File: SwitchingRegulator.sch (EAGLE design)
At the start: 30 parts, among them J1 APP_2POS_CONFIG5V_HORIZ, J2 APP_2POS_CONFIG5V_HORIZ, J4 APP_2POS_CONFIG12V_HORIZ, Q2 Q_CSD18532KCSPCB, Q3 Q_CSD18532KCSPCB, U1 OKI-78SR-5/1.5-W36HC

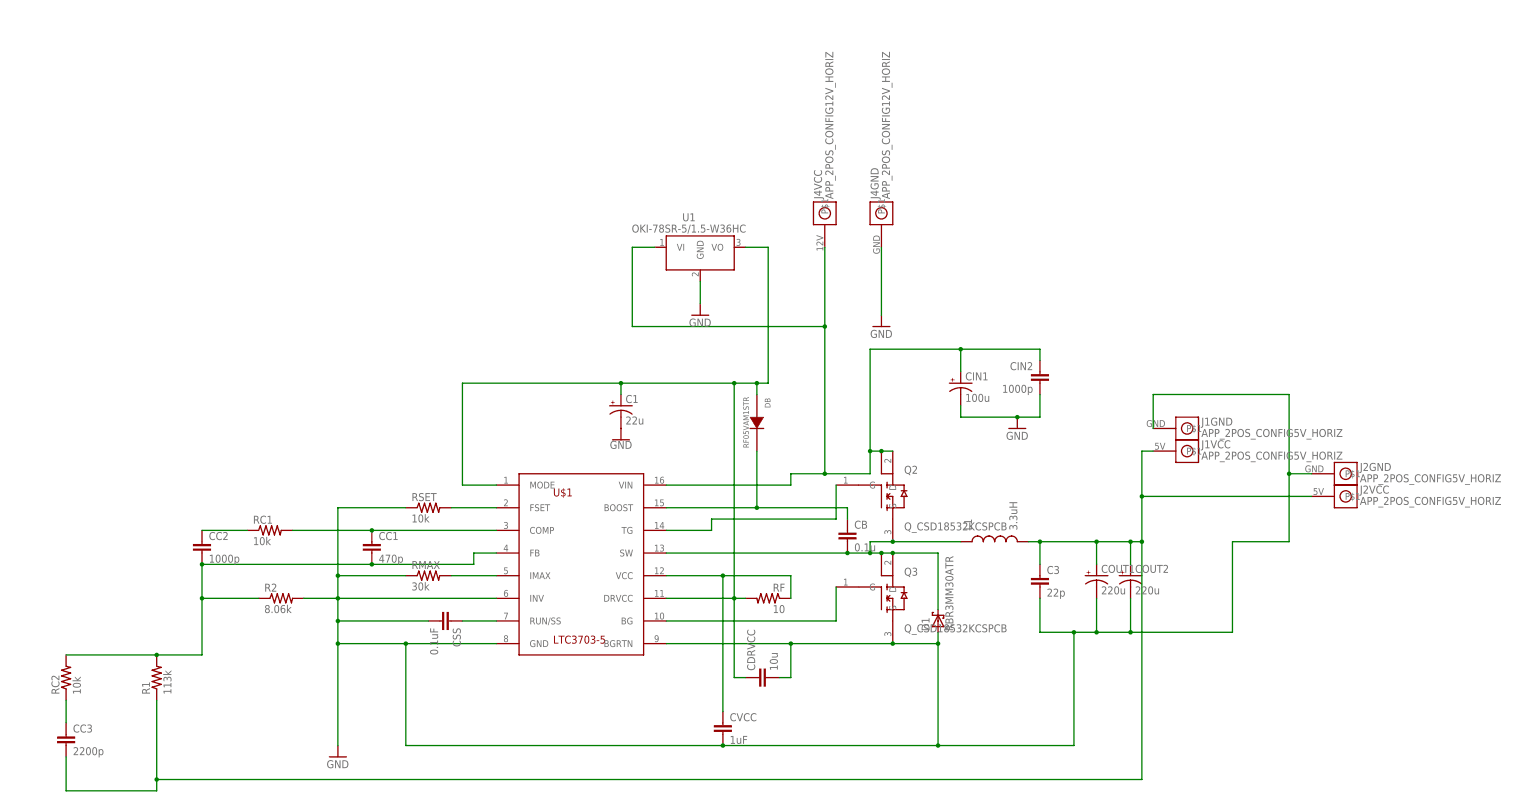
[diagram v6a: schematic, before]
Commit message: Major revision, moved LTC to bottom
Changed signal traces to be much closer to LTC chip.  Modified via stitching to cover whole polygon rather than edges only.  No more vias under IC.  Moved inductor to top side of board to prevent LTC from heating up due to MOSFET heat.  Added silkscreen stuff.  More fine details to come
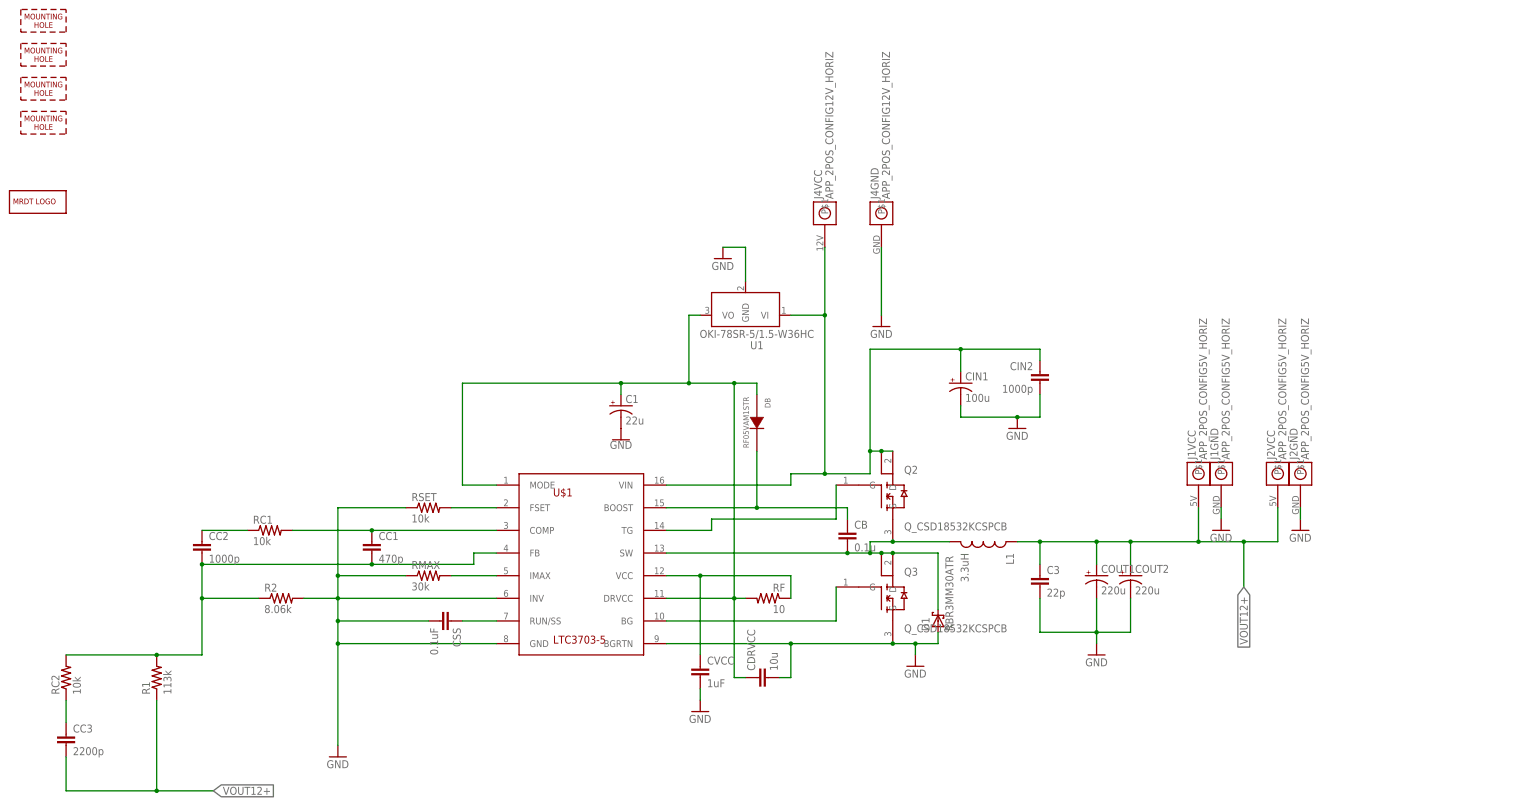
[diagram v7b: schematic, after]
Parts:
- added H1, H2, H3, H4: MOUNTING_HOLE#8, MRDT-Hardware:MOUNTING_HOLE#8
- added LOGO1: MRDT_LOGO, MRDT-Hardware:MRDT_LOGO
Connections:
- net N$15 renamed 5V
- net N$17: now also L1.2; no longer L1.1
- net VOUT12+: now also L1.1; no longer L1.2
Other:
- moved on the sheet: CVCC, J1GND, J1VCC, J2GND, J2VCC, L1, U1

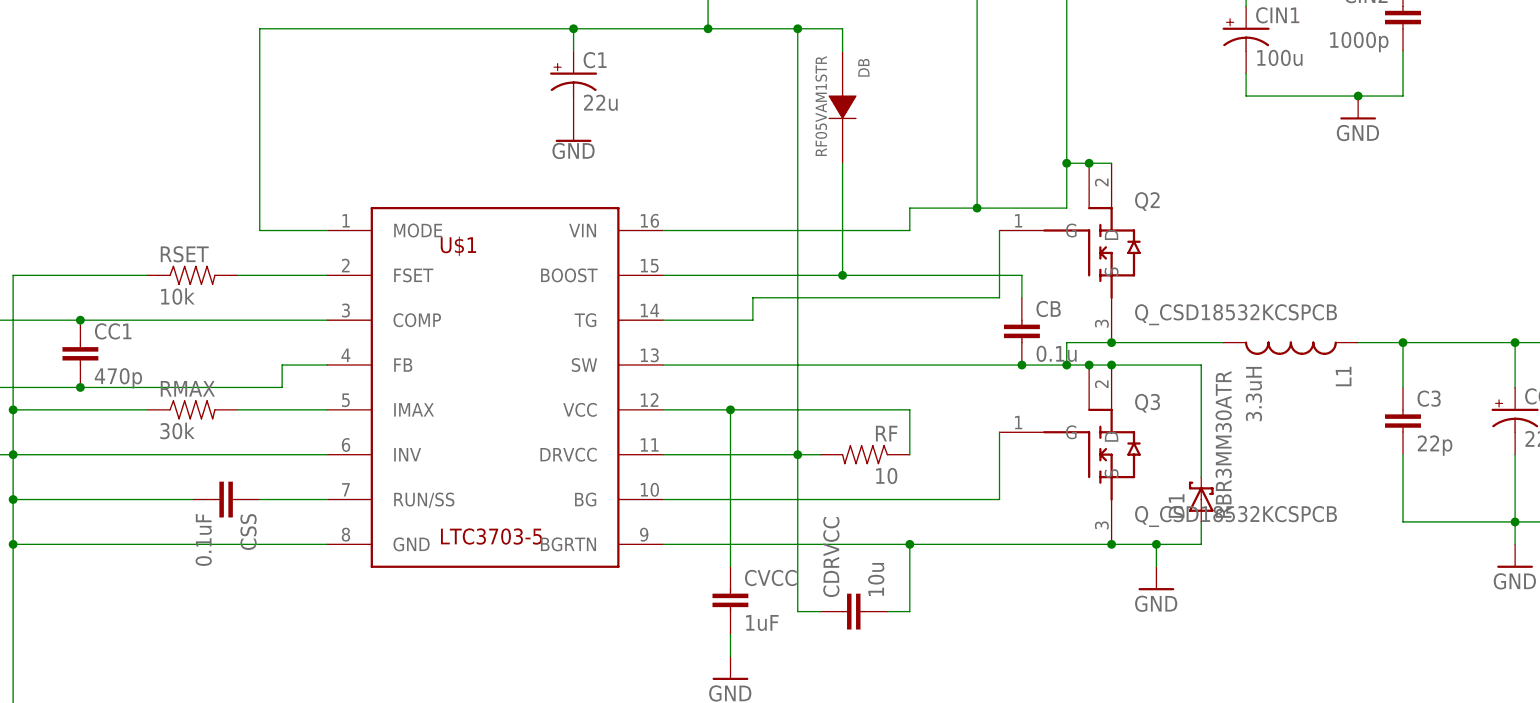
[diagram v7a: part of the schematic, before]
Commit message: Switched to upright mosfets, adjusted board accordingly
Spread out some of the signal components on the bottom side of the board.  Adjusted power planes to compensate for new mosfet orientation.
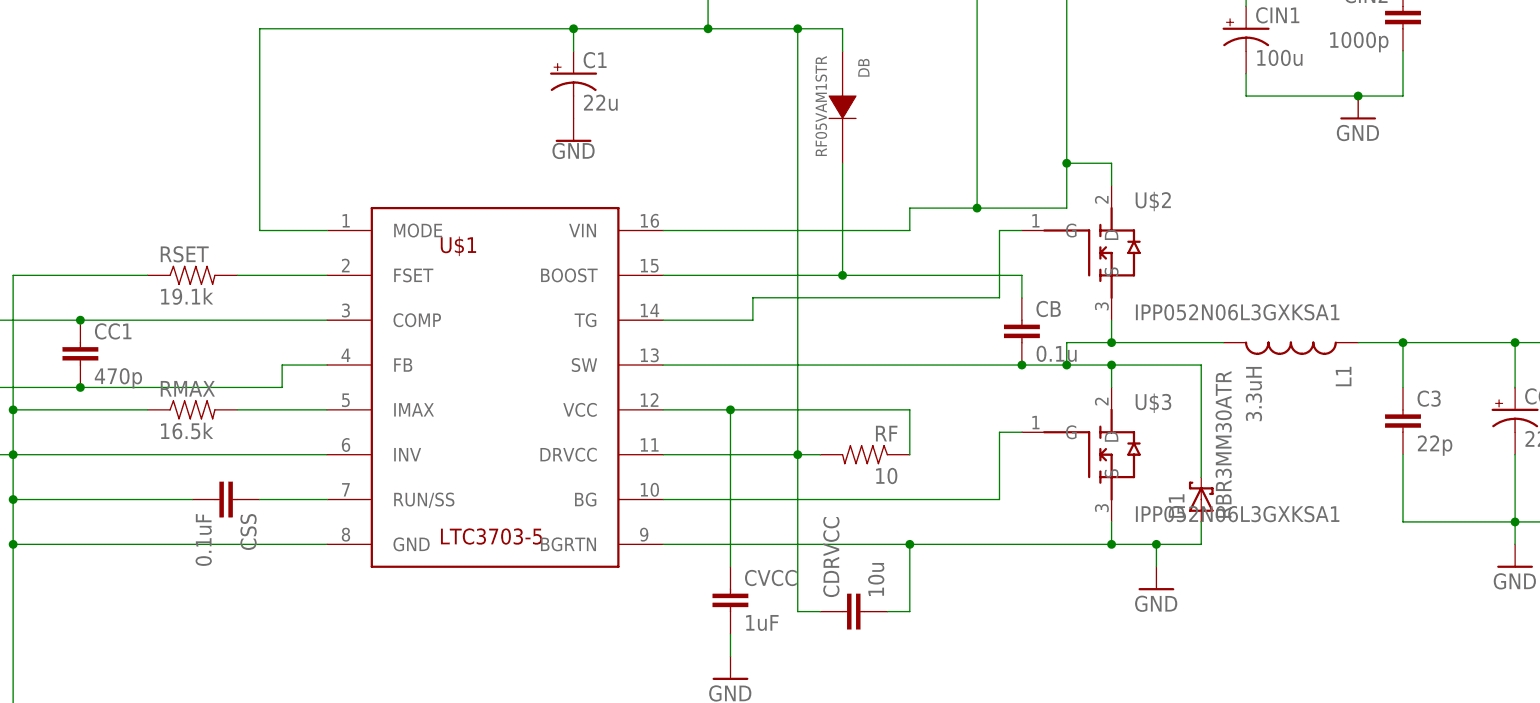
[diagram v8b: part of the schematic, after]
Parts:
- removed Q2, Q3: Q_CSD18532KCSPCB, MRDT-2014-All:Q_CSD18532KCSPCB
- added U$2, U$3: IPP052N06L3GXKSA1, buckconverter:IPP052N06L3GXKSA1
- RMAX: value 30k -> 16.5k
- RSET: value 10k -> 19.1k
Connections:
- net GND: now also U$3.S; no longer Q3.S
- net N$16: now also U$3.G; no longer Q3.G
- net N$17: now also U$2.S, U$3.D; no longer Q2.S, Q3.D, Q3.P$1
- net N$2: now also U$2.G; no longer Q2.G
- net VBATT: now also U$2.D; no longer Q2.D, Q2.P$1
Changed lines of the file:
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@@
 <?xml version="1.0" encoding="utf-8"?>
 <!DOCTYPE eagle SYSTEM "eagle.dtd">
-<eagle version="8.2.2">
+<eagle version="8.4.0">
 <drawing>
 <settings>
 <setting alwaysvectorfont="no"/>
+<setting keepoldvectorfont="yes"/>
 <setting verticaltext="up"/>
 </settings>
@@
 <part name="R2" library="SparkFun-Passives" deviceset="RESISTOR" device="0603-RES" value="8.06k"/>
 <part name="RC1" library="SparkFun-Passives" deviceset="RESISTOR" device="0603-RES" value="10k"/>
-<part name="RMAX" library="SparkFun-Passives" deviceset="RESISTOR" device="0603-RES" value="30k"/>
-<part name="RSET" library="SparkFun-Passives" deviceset="RESISTOR" device="0603-RES" value="10k"/>
+<part name="RMAX" library="SparkFun-Passives" deviceset="RESISTOR" device="0603-RES" value="16.5k"/>
+<part name="RSET" library="SparkFun-Passives" deviceset="RESISTOR" device="0603-RES" value="19.1k"/>
 <part name="U$1" library="MRDT-ICs" deviceset="LTC3703-5" device=""/>
 <part name="RC2" library="SparkFun-Passives" deviceset="RESISTOR" device="0603-RES" value="10k"/>
@@
 <part name="J1" library="MRDT-Connectors" deviceset="APP_2POS_CONFIG" device="5V_HORIZ"/>
 <part name="J2" library="MRDT-Connectors" deviceset="APP_2POS_CONFIG" device="5V_HORIZ"/>
-<part name="Q2" library="MRDT-2014-All" deviceset="Q_CSD18532KCS" device="PCB"/>
 <part name="C1" library="buckconverter" deviceset="UCZ1K220MCL1GS" device="" value="22u"/>
 <part name="GND2" library="SparkFun-PowerSymbols" deviceset="GND" device=""/>
@@
 <part name="COUT2" library="buckconverter" deviceset="EGPD101ELL221MK25H" device="" value="220u"/>
 <part name="CIN1" library="buckconverter" deviceset="B41858C9107M000" device="" value="100u"/>
-<part name="Q3" library="MRDT-2014-All" deviceset="Q_CSD18532KCS" device="PCB"/>
 <part name="D1" library="buckconverter" deviceset="RBR3MM30ATR" device=""/>
 <part name="DB" library="buckconverter" deviceset="RF05VAM1STR" device=""/>
@@
 <part name="H4" library="MRDT-Hardware" deviceset="MOUNTING_HOLE" device="#8"/>
 <part name="LOGO1" library="MRDT-Hardware" deviceset="MRDT_LOGO" device=""/>
+<part name="U$2" library="buckconverter" deviceset="IPP052N06L3GXKSA1" device=""/>
+<part name="U$3" library="buckconverter" deviceset="IPP052N06L3GXKSA1" device=""/>
 </parts>
 <sheets>
@@
 <instance part="J2" gate="GND" x="246.38" y="137.16" rot="R90"/>
 <instance part="J2" gate="VCC" x="241.3" y="137.16" rot="R90"/>
-<instance part="Q2" gate="G$1" x="154.94" y="132.08"/>
 <instance part="C1" gate="G$1" x="93.98" y="149.86"/>
 <instance part="GND2" gate="1" x="93.98" y="144.78"/>
@@
 <instance part="COUT2" gate="G$1" x="208.28" y="111.76"/>
 <instance part="CIN1" gate="G$1" x="170.18" y="154.94"/>
-<instance part="Q3" gate="G$1" x="154.94" y="109.22"/>
 <instance part="D1" gate="G$1" x="165.1" y="104.14" rot="R90"/>
 <instance part="DB" gate="G$1" x="124.46" y="147.32" rot="R270"/>
@@
 <instance part="H4" gate="G$1" x="-40.64" y="213.36"/>
 <instance part="LOGO1" gate="G$1" x="-43.18" y="195.58"/>
+<instance part="U$2" gate="G$1" x="152.4" y="132.08"/>
+<instance part="U$3" gate="G$1" x="152.4" y="109.22"/>
 </instances>
 <busses>
@@
 <wire x1="165.1" y1="99.06" x2="160.02" y2="99.06" width="0.1524" layer="91"/>
 <wire x1="160.02" y1="99.06" x2="154.94" y2="99.06" width="0.1524" layer="91"/>
+<pinref part="GND8" gate="1" pin="GND"/>
 <wire x1="154.94" y1="99.06" x2="132.08" y2="99.06" width="0.1524" layer="91"/>
-<pinref part="Q3" gate="G$1" pin="S"/>
-<junction x="154.94" y="99.06"/>
-<pinref part="GND8" gate="1" pin="GND"/>
 <wire x1="160.02" y1="96.52" x2="160.02" y2="99.06" width="0.1524" layer="91"/>
 <junction x="160.02" y="99.06"/>
+<pinref part="U$3" gate="G$1" pin="S"/>
+<wire x1="154.94" y1="101.6" x2="154.94" y2="99.06" width="0.1524" layer="91"/>
+<junction x="154.94" y="99.06"/>
 </segment>
 <segment>
@@
 <pinref part="U$1" gate="G$1" pin="BG"/>
 <wire x1="104.14" y1="104.14" x2="142.24" y2="104.14" width="0.1524" layer="91"/>
-<pinref part="Q3" gate="G$1" pin="G"/>
 <wire x1="142.24" y1="111.76" x2="142.24" y2="104.14" width="0.1524" layer="91"/>
+<pinref part="U$3" gate="G$1" pin="G"/>
+<wire x1="142.24" y1="111.76" x2="144.78" y2="111.76" width="0.1524" layer="91"/>
 </segment>
 </net>
@@
 <wire x1="165.1" y1="106.68" x2="165.1" y2="119.38" width="0.1524" layer="91"/>
 <wire x1="165.1" y1="119.38" x2="154.94" y2="119.38" width="0.1524" layer="91"/>
-<wire x1="154.94" y1="119.38" x2="152.4" y2="119.38" width="0.1524" layer="91"/>
-<wire x1="152.4" y1="119.38" x2="149.86" y2="119.38" width="0.1524" layer="91"/>
-<wire x1="154.94" y1="121.92" x2="149.86" y2="121.92" width="0.1524" layer="91"/>
+<wire x1="154.94" y1="119.38" x2="149.86" y2="119.38" width="0.1524" layer="91"/>
 <wire x1="149.86" y1="121.92" x2="149.86" y2="119.38" width="0.1524" layer="91"/>
 <pinref part="CB" gate="G$1" pin="2"/>
 <junction x="144.78" y="119.38"/>
-<pinref part="Q2" gate="G$1" pin="S"/>
-<pinref part="Q3" gate="G$1" pin="D"/>
-<junction x="154.94" y="119.38"/>
-<pinref part="Q3" gate="G$1" pin="P$1"/>
-<junction x="152.4" y="119.38"/>
 <pinref part="D1" gate="G$1" pin="C"/>
 <junction x="149.86" y="119.38"/>
 <pinref part="L1" gate="G$1" pin="2"/>
 <wire x1="167.64" y1="121.92" x2="154.94" y2="121.92" width="0.1524" layer="91"/>
+<pinref part="U$2" gate="G$1" pin="S"/>
+<wire x1="154.94" y1="121.92" x2="149.86" y2="121.92" width="0.1524" layer="91"/>
+<wire x1="154.94" y1="124.46" x2="154.94" y2="121.92" width="0.1524" layer="91"/>
 <junction x="154.94" y="121.92"/>
+<pinref part="U$3" gate="G$1" pin="D"/>
+<wire x1="154.94" y1="116.84" x2="154.94" y2="119.38" width="0.1524" layer="91"/>
+<junction x="154.94" y="119.38"/>
 </segment>
 </net>
@@
 <wire x1="114.3" y1="124.46" x2="114.3" y2="127" width="0.1524" layer="91"/>
 <wire x1="114.3" y1="127" x2="142.24" y2="127" width="0.1524" layer="91"/>
-<pinref part="Q2" gate="G$1" pin="G"/>
 <wire x1="142.24" y1="134.62" x2="142.24" y2="127" width="0.1524" layer="91"/>
+<pinref part="U$2" gate="G$1" pin="G"/>
+<wire x1="144.78" y1="134.62" x2="142.24" y2="134.62" width="0.1524" layer="91"/>
 </segment>
 </net>
@@
 <wire x1="170.18" y1="165.1" x2="149.86" y2="165.1" width="0.1524" layer="91"/>
 <wire x1="149.86" y1="165.1" x2="149.86" y2="142.24" width="0.1524" layer="91"/>
-<pinref part="Q2" gate="G$1" pin="P$1"/>
 <wire x1="149.86" y1="142.24" x2="149.86" y2="137.16" width="0.1524" layer="91"/>
-<wire x1="152.4" y1="142.24" x2="149.86" y2="142.24" width="0.1524" layer="91"/>
-<pinref part="Q2" gate="G$1" pin="D"/>
-<wire x1="154.94" y1="142.24" x2="152.4" y2="142.24" width="0.1524" layer="91"/>
+<wire x1="154.94" y1="142.24" x2="149.86" y2="142.24" width="0.1524" layer="91"/>
 <junction x="139.7" y="137.16"/>
 <junction x="149.86" y="142.24"/>
-<junction x="152.4" y="142.24"/>
 <junction x="170.18" y="165.1"/>
 <pinref part="J4" gate="VCC" pin="P$1"/>
@@
 <wire x1="132.08" y1="172.72" x2="139.7" y2="172.72" width="0.1524" layer="91"/>
 <junction x="139.7" y="172.72"/>
-</segment>
-</net>
+<pinref part="U$2" gate="G$1" pin="D"/>
+<wire x1="154.94" y1="142.24" x2="154.94" y2="139.7" width="0.1524" layer="91"/>
+</segment>
+</net>
